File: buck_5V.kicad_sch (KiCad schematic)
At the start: 14 parts, among them U3 TPS566238PRQFR

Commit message: WIP v0.2.0 changes
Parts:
- added R79: 10k, Resistor_SMD:R_0603_1608Metric_Pad0.98x0.95mm_HandSolder, symbol Device:R_Small
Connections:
- net EN: now also R79.1
- net GND: now also R79.2
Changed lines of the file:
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@@
+	(wire
+		(pts
+			(xy 87.63 129.54) (xy 87.63 133.35)
+		)
+		(stroke
+			(width 0)
+			(type default)
+		)
+	)
 	(wire
 		(pts
@@
 	(wire
 		(pts
+			(xy 87.63 119.38) (xy 85.09 119.38)
+		)
+		(stroke
+			(width 0)
+			(type default)
+		)
+	)
+	(wire
+		(pts
 			(xy 204.47 72.39) (xy 215.9 72.39)
 		)
@@
 		(pts
 			(xy 215.9 83.82) (xy 222.25 83.82)
+		)
+		(stroke
+			(width 0)
+			(type default)
+		)
+	)
+	(wire
+		(pts
+			(xy 87.63 124.46) (xy 87.63 119.38)
 		)
 		(stroke
@@
 		(shape input)
 		(at 27.94 67.31 180)
+		(effects
+			(font
+				(size 1.27 1.27)
+			)
+			(justify right)
+		)
+	)
+	(hierarchical_label "EN"
+		(shape input)
+		(at 85.09 119.38 180)
 		(effects
 			(font
@@
 		(on_board yes)
 		(dnp no)
-		(property "Reference" "#PWR072"
+		(property "Reference" "#PWR071"
 			(at 191.77 96.52 0)
 			(effects
@@
 			(project "HALSPA"
 				(path "/7eeba806-440e-4671-bc07-69fe183910a7/8a7bd3c3-3783-4a08-9c22-bb373aae5663/3b017fe7-4da4-47f0-996e-c80c0d6dd0eb"
-					(reference "#PWR072")
+					(reference "#PWR071")
 					(unit 1)
 				)
@@
 		(on_board yes)
 		(dnp no)
-		(property "Reference" "#PWR073"
+		(property "Reference" "#PWR072"
 			(at 204.47 101.6 0)
 			(effects
@@
 			(project "HALSPA"
 				(path "/7eeba806-440e-4671-bc07-69fe183910a7/8a7bd3c3-3783-4a08-9c22-bb373aae5663/3b017fe7-4da4-47f0-996e-c80c0d6dd0eb"
-					(reference "#PWR073")
+					(reference "#PWR072")
 					(unit 1)
 				)
@@
 		(on_board yes)
 		(dnp no)
-		(property "Reference" "#PWR069"
+		(property "Reference" "#PWR068"
 			(at 102.87 109.22 0)
 			(effects
@@
 			(project "HALSPA"
 				(path "/7eeba806-440e-4671-bc07-69fe183910a7/8a7bd3c3-3783-4a08-9c22-bb373aae5663/3b017fe7-4da4-47f0-996e-c80c0d6dd0eb"
-					(reference "#PWR069")
+					(reference "#PWR068")
 					(unit 1)
 				)
@@
 	)
 	(symbol
+		(lib_id "Device:R_Small")
+		(at 87.63 127 0)
+		(unit 1)
+		(exclude_from_sim no)
+		(in_bom yes)
+		(on_board yes)
+		(dnp no)
+		(fields_autoplaced yes)
+		(property "Reference" "R79"
+			(at 90.17 125.7299 0)
+			(effects
+				(font
+					(size 1.016 1.016)
+				)
+				(justify left)
+			)
+		)
+		(property "Value" "10k"
+			(at 90.17 128.2699 0)
+			(effects
+				(font
+					(size 1.27 1.27)
+				)
+				(justify left)
+			)
+		)
+		(property "Footprint" "Resistor_SMD:R_0603_1608Metric_Pad0.98x0.95mm_HandSolder"
+			(at 87.63 127 0)
+			(effects
+				(font
+					(size 1.27 1.27)
+				)
+				(hide yes)
+			)
+		)
+		(property "Datasheet" "~"
+			(at 87.63 127 0)
+			(effects
+				(font
+					(size 1.27 1.27)
+				)
+				(hide yes)
+			)
+		)
+		(property "Description" "Resistor, small symbol"
+			(at 87.63 127 0)
+			(effects
+				(font
+					(size 1.27 1.27)
+				)
+				(hide yes)
+			)
+		)
+		(property "LCSC" "C25804"
+			(at 87.63 127 0)
+			(effects
+				(font
+					(size 1.27 1.27)
+				)
+			)
+		)
+		(pin "1"
+		)
+		(pin "2"
+		)
+		(instances
+			(project "HALSPA"
+				(path "/7eeba806-440e-4671-bc07-69fe183910a7/8a7bd3c3-3783-4a08-9c22-bb373aae5663/3b017fe7-4da4-47f0-996e-c80c0d6dd0eb"
+					(reference "R79")
+					(unit 1)
+				)
+			)
+		)
+	)
+	(symbol
 		(lib_id "power:PWR_FLAG")
 		(at 195.58 72.39 0)
@@
 		(on_board yes)
 		(dnp no)
-		(property "Reference" "#PWR067"
+		(property "Reference" "#PWR066"
 			(at 50.8 93.98 0)
 			(effects
@@
 			(project "HALSPA"
 				(path "/7eeba806-440e-4671-bc07-69fe183910a7/8a7bd3c3-3783-4a08-9c22-bb373aae5663/3b017fe7-4da4-47f0-996e-c80c0d6dd0eb"
-					(reference "#PWR067")
+					(reference "#PWR066")
 					(unit 1)
 				)
@@
 		(on_board yes)
 		(dnp no)
-		(property "Reference" "#PWR066"
+		(property "Reference" "#PWR065"
 			(at 36.83 93.98 0)
 			(effects
@@
 			(project "HALSPA"
 				(path "/7eeba806-440e-4671-bc07-69fe183910a7/8a7bd3c3-3783-4a08-9c22-bb373aae5663/3b017fe7-4da4-47f0-996e-c80c0d6dd0eb"
-					(reference "#PWR066")
+					(reference "#PWR065")
 					(unit 1)
 				)
@@
 		(on_board yes)
 		(dnp no)
-		(property "Reference" "#PWR071"
+		(property "Reference" "#PWR070"
 			(at 172.72 96.52 0)
 			(effects
@@
 			(project "HALSPA"
 				(path "/7eeba806-440e-4671-bc07-69fe183910a7/8a7bd3c3-3783-4a08-9c22-bb373aae5663/3b017fe7-4da4-47f0-996e-c80c0d6dd0eb"
-					(reference "#PWR071")
+					(reference "#PWR070")
 					(unit 1)
 				)
@@
 		(on_board yes)
 		(dnp no)
-		(property "Reference" "#PWR070"
+		(property "Reference" "#PWR069"
 			(at 162.56 96.52 0)
 			(effects
@@
 			(project "HALSPA"
 				(path "/7eeba806-440e-4671-bc07-69fe183910a7/8a7bd3c3-3783-4a08-9c22-bb373aae5663/3b017fe7-4da4-47f0-996e-c80c0d6dd0eb"
-					(reference "#PWR070")
+					(reference "#PWR069")
+					(unit 1)
+				)
+			)
+		)
+	)
+	(symbol
+		(lib_id "power:GND")
+		(at 87.63 133.35 0)
+		(mirror y)
+		(unit 1)
+		(exclude_from_sim no)
+		(in_bom yes)
+		(on_board yes)
+		(dnp no)
+		(fields_autoplaced yes)
+		(property "Reference" "#PWR0217"
+			(at 87.63 139.7 0)
+			(effects
+				(font
+					(size 1.27 1.27)
+				)
+				(hide yes)
+			)
+		)
+		(property "Value" "GND"
+			(at 87.63 138.43 0)
+			(effects
+				(font
+					(size 1.27 1.27)
+				)
+			)
+		)
+		(property "Footprint" ""
+			(at 87.63 133.35 0)
+			(effects
+				(font
+					(size 1.27 1.27)
+				)
+				(hide yes)
+			)
+		)
+		(property "Datasheet" ""
+			(at 87.63 133.35 0)
+			(effects
+				(font
+					(size 1.27 1.27)
+				)
+				(hide yes)
+			)
+		)
+		(property "Description" "Power symbol creates a global label with name \"GND\" , ground"
+			(at 87.63 133.35 0)
+			(effects
+				(font
+					(size 1.27 1.27)
+				)
+				(hide yes)
+			)
+		)
+		(pin "1"
+		)
+		(instances
+			(project "HALSPA"
+				(path "/7eeba806-440e-4671-bc07-69fe183910a7/8a7bd3c3-3783-4a08-9c22-bb373aae5663/3b017fe7-4da4-47f0-996e-c80c0d6dd0eb"
+					(reference "#PWR0217")
 					(unit 1)
 				)
@@
 		(on_board yes)
 		(dnp no)
-		(property "Reference" "#PWR068"
+		(property "Reference" "#PWR067"
 			(at 67.31 109.22 0)
 			(effects
@@
 			(project "HALSPA"
 				(path "/7eeba806-440e-4671-bc07-69fe183910a7/8a7bd3c3-3783-4a08-9c22-bb373aae5663/3b017fe7-4da4-47f0-996e-c80c0d6dd0eb"
-					(reference "#PWR068")
+					(reference "#PWR067")
 					(unit 1)
 				)

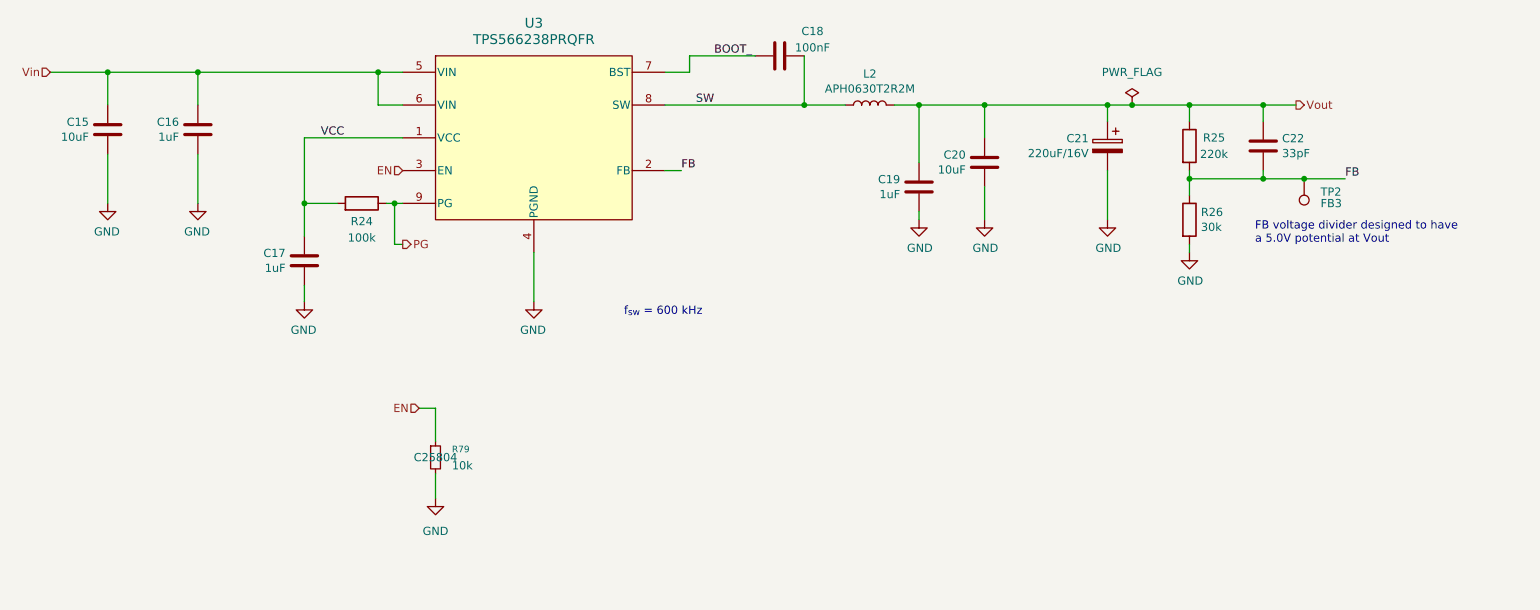
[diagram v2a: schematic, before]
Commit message: Assign part numbers and finish other 0.2.0 changes
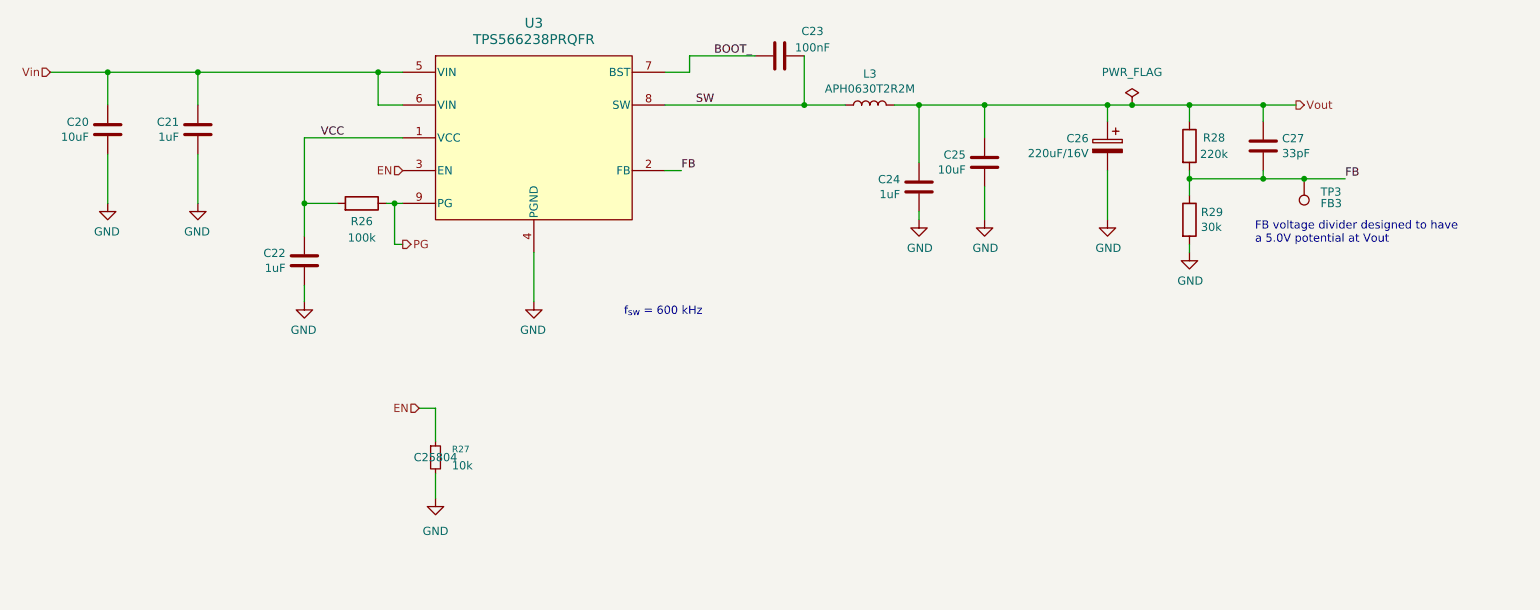
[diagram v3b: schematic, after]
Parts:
- renumbered C15 to C20, C16 to C21, C17 to C22, C18 to C23, C19 to C24, C20 to C25, C21 to C26, C22 to C27, L2 to L3, R24 to R26, R79 to R27, R25 to R28, R26 to R29, TP2 to TP3
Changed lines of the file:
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@@
 		(on_board yes)
 		(dnp no)
-		(property "Reference" "#PWR071"
+		(property "Reference" "#PWR078"
 			(at 191.77 96.52 0)
 			(effects
@@
 			(project "HALSPA"
 				(path "/7eeba806-440e-4671-bc07-69fe183910a7/8a7bd3c3-3783-4a08-9c22-bb373aae5663/3b017fe7-4da4-47f0-996e-c80c0d6dd0eb"
-					(reference "#PWR071")
+					(reference "#PWR078")
 					(unit 1)
 				)
@@
 		(on_board yes)
 		(dnp no)
-		(property "Reference" "#PWR072"
+		(property "Reference" "#PWR079"
 			(at 204.47 101.6 0)
 			(effects
@@
 			(project "HALSPA"
 				(path "/7eeba806-440e-4671-bc07-69fe183910a7/8a7bd3c3-3783-4a08-9c22-bb373aae5663/3b017fe7-4da4-47f0-996e-c80c0d6dd0eb"
-					(reference "#PWR072")
+					(reference "#PWR079")
 					(unit 1)
 				)
@@
 		(on_board yes)
 		(dnp no)
-		(property "Reference" "C19"
+		(property "Reference" "C24"
 			(at 159.639 83.9216 0)
 			(effects
@@
 			(project "HALSPA"
 				(path "/7eeba806-440e-4671-bc07-69fe183910a7/8a7bd3c3-3783-4a08-9c22-bb373aae5663/3b017fe7-4da4-47f0-996e-c80c0d6dd0eb"
-					(reference "C19")
+					(reference "C24")
 					(unit 1)
 				)
@@
 		(on_board yes)
 		(dnp no)
-		(property "Reference" "#PWR068"
+		(property "Reference" "#PWR075"
 			(at 102.87 109.22 0)
 			(effects
@@
 			(project "HALSPA"
 				(path "/7eeba806-440e-4671-bc07-69fe183910a7/8a7bd3c3-3783-4a08-9c22-bb373aae5663/3b017fe7-4da4-47f0-996e-c80c0d6dd0eb"
-					(reference "#PWR068")
+					(reference "#PWR075")
 					(unit 1)
 				)
@@
 		(on_board yes)
 		(dnp no)
-		(property "Reference" "R24"
+		(property "Reference" "R26"
 			(at 76.2 90.424 90)
 			(effects
@@
 			(project "HALSPA"
 				(path "/7eeba806-440e-4671-bc07-69fe183910a7/8a7bd3c3-3783-4a08-9c22-bb373aae5663/3b017fe7-4da4-47f0-996e-c80c0d6dd0eb"
-					(reference "R24")
+					(reference "R26")
 					(unit 1)
 				)
@@
 		(dnp no)
 		(fields_autoplaced yes)
-		(property "Reference" "R79"
+		(property "Reference" "R27"
 			(at 90.17 125.7299 0)
 			(effects
@@
 			(project "HALSPA"
 				(path "/7eeba806-440e-4671-bc07-69fe183910a7/8a7bd3c3-3783-4a08-9c22-bb373aae5663/3b017fe7-4da4-47f0-996e-c80c0d6dd0eb"
-					(reference "R79")
+					(reference "R27")
 					(unit 1)
 				)
@@
 		(dnp no)
 		(fields_autoplaced yes)
-		(property "Reference" "#FLG07"
+		(property "Reference" "#FLG08"
 			(at 195.58 70.485 0)
 			(effects
@@
 			(project "HALSPA"
 				(path "/7eeba806-440e-4671-bc07-69fe183910a7/8a7bd3c3-3783-4a08-9c22-bb373aae5663/3b017fe7-4da4-47f0-996e-c80c0d6dd0eb"
-					(reference "#FLG07")
+					(reference "#FLG08")
 					(unit 1)
 				)
@@
 		(on_board yes)
 		(dnp no)
-		(property "Reference" "TP2"
+		(property "Reference" "TP3"
 			(at 224.79 85.8519 0)
 			(effects
@@
 			(project "HALSPA"
 				(path "/7eeba806-440e-4671-bc07-69fe183910a7/8a7bd3c3-3783-4a08-9c22-bb373aae5663/3b017fe7-4da4-47f0-996e-c80c0d6dd0eb"
-					(reference "TP2")
+					(reference "TP3")
 					(unit 1)
 				)
@@
 		(on_board yes)
 		(dnp no)
-		(property "Reference" "R26"
+		(property "Reference" "R29"
 			(at 206.248 89.0016 0)
 			(effects
@@
 			(project "HALSPA"
 				(path "/7eeba806-440e-4671-bc07-69fe183910a7/8a7bd3c3-3783-4a08-9c22-bb373aae5663/3b017fe7-4da4-47f0-996e-c80c0d6dd0eb"
-					(reference "R26")
+					(reference "R29")
 					(unit 1)
 				)
@@
 		(on_board yes)
 		(dnp no)
-		(property "Reference" "#PWR066"
+		(property "Reference" "#PWR072"
 			(at 50.8 93.98 0)
 			(effects
@@
 			(project "HALSPA"
 				(path "/7eeba806-440e-4671-bc07-69fe183910a7/8a7bd3c3-3783-4a08-9c22-bb373aae5663/3b017fe7-4da4-47f0-996e-c80c0d6dd0eb"
-					(reference "#PWR066")
+					(reference "#PWR072")
 					(unit 1)
 				)
@@
 		(on_board yes)
 		(dnp no)
-		(property "Reference" "L2"
+		(property "Reference" "L3"
 			(at 154.94 67.564 90)
 			(effects
@@
 			(project "HALSPA"
 				(path "/7eeba806-440e-4671-bc07-69fe183910a7/8a7bd3c3-3783-4a08-9c22-bb373aae5663/3b017fe7-4da4-47f0-996e-c80c0d6dd0eb"
-					(reference "L2")
+					(reference "L3")
 					(unit 1)
 				)
@@
 		(on_board yes)
 		(dnp no)
-		(property "Reference" "R25"
+		(property "Reference" "R28"
 			(at 208.28 77.47 0)
 			(effects
@@
 			(project "HALSPA"
 				(path "/7eeba806-440e-4671-bc07-69fe183910a7/8a7bd3c3-3783-4a08-9c22-bb373aae5663/3b017fe7-4da4-47f0-996e-c80c0d6dd0eb"
-					(reference "R25")
+					(reference "R28")
 					(unit 1)
 				)
@@
 		(on_board yes)
 		(dnp no)
-		(property "Reference" "#PWR065"
+		(property "Reference" "#PWR071"
 			(at 36.83 93.98 0)
 			(effects
@@
 			(project "HALSPA"
 				(path "/7eeba806-440e-4671-bc07-69fe183910a7/8a7bd3c3-3783-4a08-9c22-bb373aae5663/3b017fe7-4da4-47f0-996e-c80c0d6dd0eb"
-					(reference "#PWR065")
+					(reference "#PWR071")
 					(unit 1)
 				)
@@
 		(on_board yes)
 		(dnp no)
-		(property "Reference" "C22"
+		(property "Reference" "C27"
 			(at 218.821 77.5716 0)
 			(effects
@@
 			(project "HALSPA"
 				(path "/7eeba806-440e-4671-bc07-69fe183910a7/8a7bd3c3-3783-4a08-9c22-bb373aae5663/3b017fe7-4da4-47f0-996e-c80c0d6dd0eb"
-					(reference "C22")
+					(reference "C27")
 					(unit 1)
 				)
@@
 		(on_board yes)
 		(dnp no)
-		(property "Reference" "C18"
+		(property "Reference" "C23"
 			(at 146.05 60.96 90)
 			(effects
@@
 			(project "HALSPA"
 				(path "/7eeba806-440e-4671-bc07-69fe183910a7/8a7bd3c3-3783-4a08-9c22-bb373aae5663/3b017fe7-4da4-47f0-996e-c80c0d6dd0eb"
-					(reference "C18")
+					(reference "C23")
 					(unit 1)
 				)
@@
 		(on_board yes)
 		(dnp no)
-		(property "Reference" "C21"
+		(property "Reference" "C26"
 			(at 188.849 77.5716 0)
 			(effects
@@
 			(project "HALSPA"
 				(path "/7eeba806-440e-4671-bc07-69fe183910a7/8a7bd3c3-3783-4a08-9c22-bb373aae5663/3b017fe7-4da4-47f0-996e-c80c0d6dd0eb"
-					(reference "C21")
+					(reference "C26")
 					(unit 1)
 				)
@@
 		(on_board yes)
 		(dnp no)
-		(property "Reference" "C17"
+		(property "Reference" "C22"
 			(at 64.389 95.3516 0)
 			(effects
@@
 			(project "HALSPA"
 				(path "/7eeba806-440e-4671-bc07-69fe183910a7/8a7bd3c3-3783-4a08-9c22-bb373aae5663/3b017fe7-4da4-47f0-996e-c80c0d6dd0eb"
-					(reference "C17")
+					(reference "C22")
 					(unit 1)
 				)
@@
 		(on_board yes)
 		(dnp no)
-		(property "Reference" "C16"
+		(property "Reference" "C21"
 			(at 47.879 75.0316 0)
 			(effects
@@
 			(project "HALSPA"
 				(path "/7eeba806-440e-4671-bc07-69fe183910a7/8a7bd3c3-3783-4a08-9c22-bb373aae5663/3b017fe7-4da4-47f0-996e-c80c0d6dd0eb"
-					(reference "C16")
+					(reference "C21")
 					(unit 1)
 				)
@@
 		(on_board yes)
 		(dnp no)
-		(property "Reference" "#PWR070"
+		(property "Reference" "#PWR077"
 			(at 172.72 96.52 0)
 			(effects
@@
 			(project "HALSPA"
 				(path "/7eeba806-440e-4671-bc07-69fe183910a7/8a7bd3c3-3783-4a08-9c22-bb373aae5663/3b017fe7-4da4-47f0-996e-c80c0d6dd0eb"
-					(reference "#PWR070")
+					(reference "#PWR077")
 					(unit 1)
 				)
@@
 		(on_board yes)
 		(dnp no)
-		(property "Reference" "C15"
+		(property "Reference" "C20"
 			(at 33.909 75.0316 0)
 			(effects
@@
 			(project "HALSPA"
 				(path "/7eeba806-440e-4671-bc07-69fe183910a7/8a7bd3c3-3783-4a08-9c22-bb373aae5663/3b017fe7-4da4-47f0-996e-c80c0d6dd0eb"
-					(reference "C15")
+					(reference "C20")
 					(unit 1)
 				)
@@
 		(on_board yes)
 		(dnp no)
-		(property "Reference" "#PWR069"
+		(property "Reference" "#PWR076"
 			(at 162.56 96.52 0)
 			(effects
@@
 			(project "HALSPA"
 				(path "/7eeba806-440e-4671-bc07-69fe183910a7/8a7bd3c3-3783-4a08-9c22-bb373aae5663/3b017fe7-4da4-47f0-996e-c80c0d6dd0eb"
-					(reference "#PWR069")
+					(reference "#PWR076")
 					(unit 1)
 				)
@@
 		(dnp no)
 		(fields_autoplaced yes)
-		(property "Reference" "#PWR0217"
+		(property "Reference" "#PWR074"
 			(at 87.63 139.7 0)
 			(effects
@@
 			(project "HALSPA"
 				(path "/7eeba806-440e-4671-bc07-69fe183910a7/8a7bd3c3-3783-4a08-9c22-bb373aae5663/3b017fe7-4da4-47f0-996e-c80c0d6dd0eb"
-					(reference "#PWR0217")
+					(reference "#PWR074")
 					(unit 1)
 				)
@@
 		(on_board yes)
 		(dnp no)
-		(property "Reference" "#PWR067"
+		(property "Reference" "#PWR073"
 			(at 67.31 109.22 0)
 			(effects
@@
 			(project "HALSPA"
 				(path "/7eeba806-440e-4671-bc07-69fe183910a7/8a7bd3c3-3783-4a08-9c22-bb373aae5663/3b017fe7-4da4-47f0-996e-c80c0d6dd0eb"
-					(reference "#PWR067")
+					(reference "#PWR073")
 					(unit 1)
 				)
@@
 		(on_board yes)
 		(dnp no)
-		(property "Reference" "C20"
+		(property "Reference" "C25"
 			(at 169.799 80.1116 0)
 			(effects
@@
 			(project "HALSPA"
 				(path "/7eeba806-440e-4671-bc07-69fe183910a7/8a7bd3c3-3783-4a08-9c22-bb373aae5663/3b017fe7-4da4-47f0-996e-c80c0d6dd0eb"
-					(reference "C20")
-					(unit 1)
-				)
+					(reference "C25")
+					(unit 1)
+				)

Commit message: Update the title blocks
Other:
- title: HALPI2 -> HALSPA - Hat Labs Spaghetti Board
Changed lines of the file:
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@@
 	(paper "A4")
 	(title_block
-		(title "HALPI2")
-		(date "2025-01-26")
-		(rev "v0.0.1")
+		(title "HALSPA - Hat Labs Spaghetti Board")
+		(date "2025-04-17")
+		(rev "v0.2.0")
 		(company "Hat Labs Oy")
-		(comment 1 "https://ohwr.org/cern_ohl_s_v2.pdf")
+		(comment 1 "See the accompanying LICENSE.md file for license details.")
 		(comment 2 "To view a copy of this license, visit ")
 		(comment 3 "HALPI2 is licensed under CERN-OHL-S v2.")

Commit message: Add JLCPCB corrections
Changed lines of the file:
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@@
 					(size 1.27 1.27)
 				)
+				(hide yes)
 			)
 		)
